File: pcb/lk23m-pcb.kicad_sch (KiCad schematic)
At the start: 59 parts, among them J1 Conn_01x02, SW1 RotaryEncoder_Switch_MP, SW10 SW_Push, SW11 SW_Push, SW12 SW_Push, SW13 SW_Push, SW14 SW_Push, SW15 SW_Push, SW16 SW_Push, SW17 SW_Push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

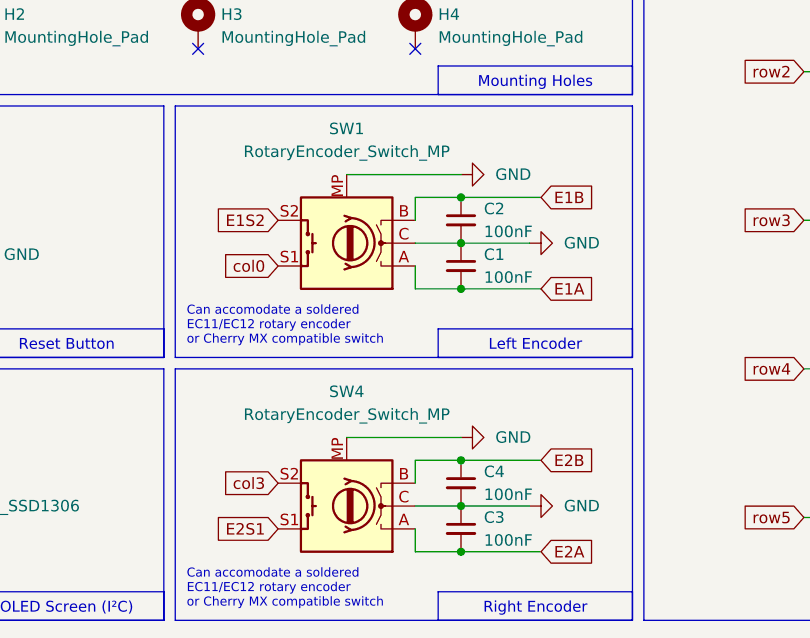
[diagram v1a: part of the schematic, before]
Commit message: Update LKBD and use new SW+Stab layout (#9)
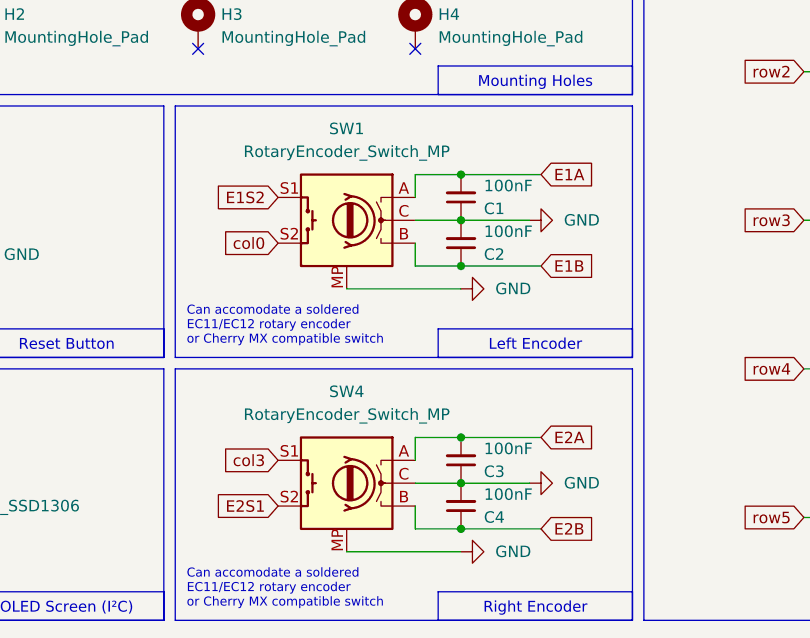
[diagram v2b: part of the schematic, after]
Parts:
- SW23: footprint LKBD_KeySwitch:SW_MX_2U_HotSwap_THT_sqSilk -> LKBD_KeySwitch:SW_MX_HotSwap_THT_sqSilk
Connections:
- net E1S2: now also SW1.S1; no longer SW1.S2
- net E2S1: now also SW4.S2; no longer SW4.S1
- net col0: now also SW1.S2; no longer SW1.S1
- net col3: now also SW4.S1; no longer SW4.S2
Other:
- moved on the sheet: C1, C2, C3, C4, SW1, SW4
